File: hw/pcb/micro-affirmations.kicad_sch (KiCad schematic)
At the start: 18 parts, among them J1 USB-C_2171750001, J2 DEBUG, SW1 SW_Push, U1 STM32C031C6Tx

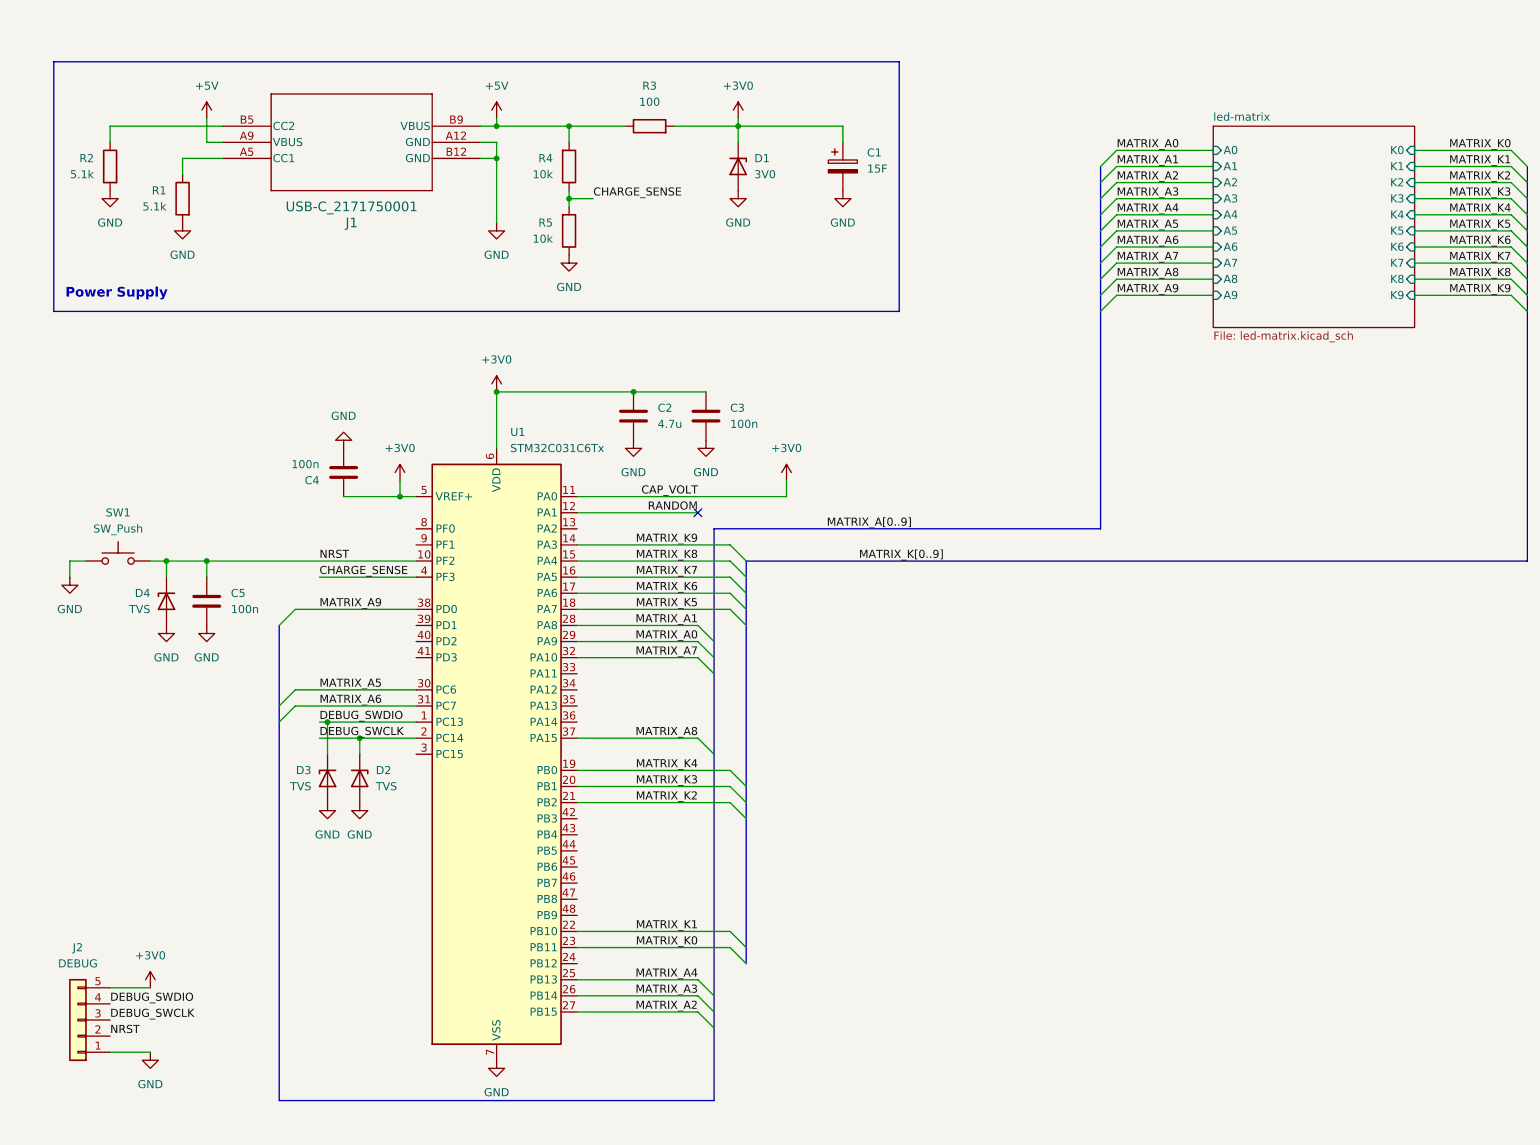
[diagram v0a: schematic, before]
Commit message: chore: redesigned pcb, new capacitor charger and smaller matrix
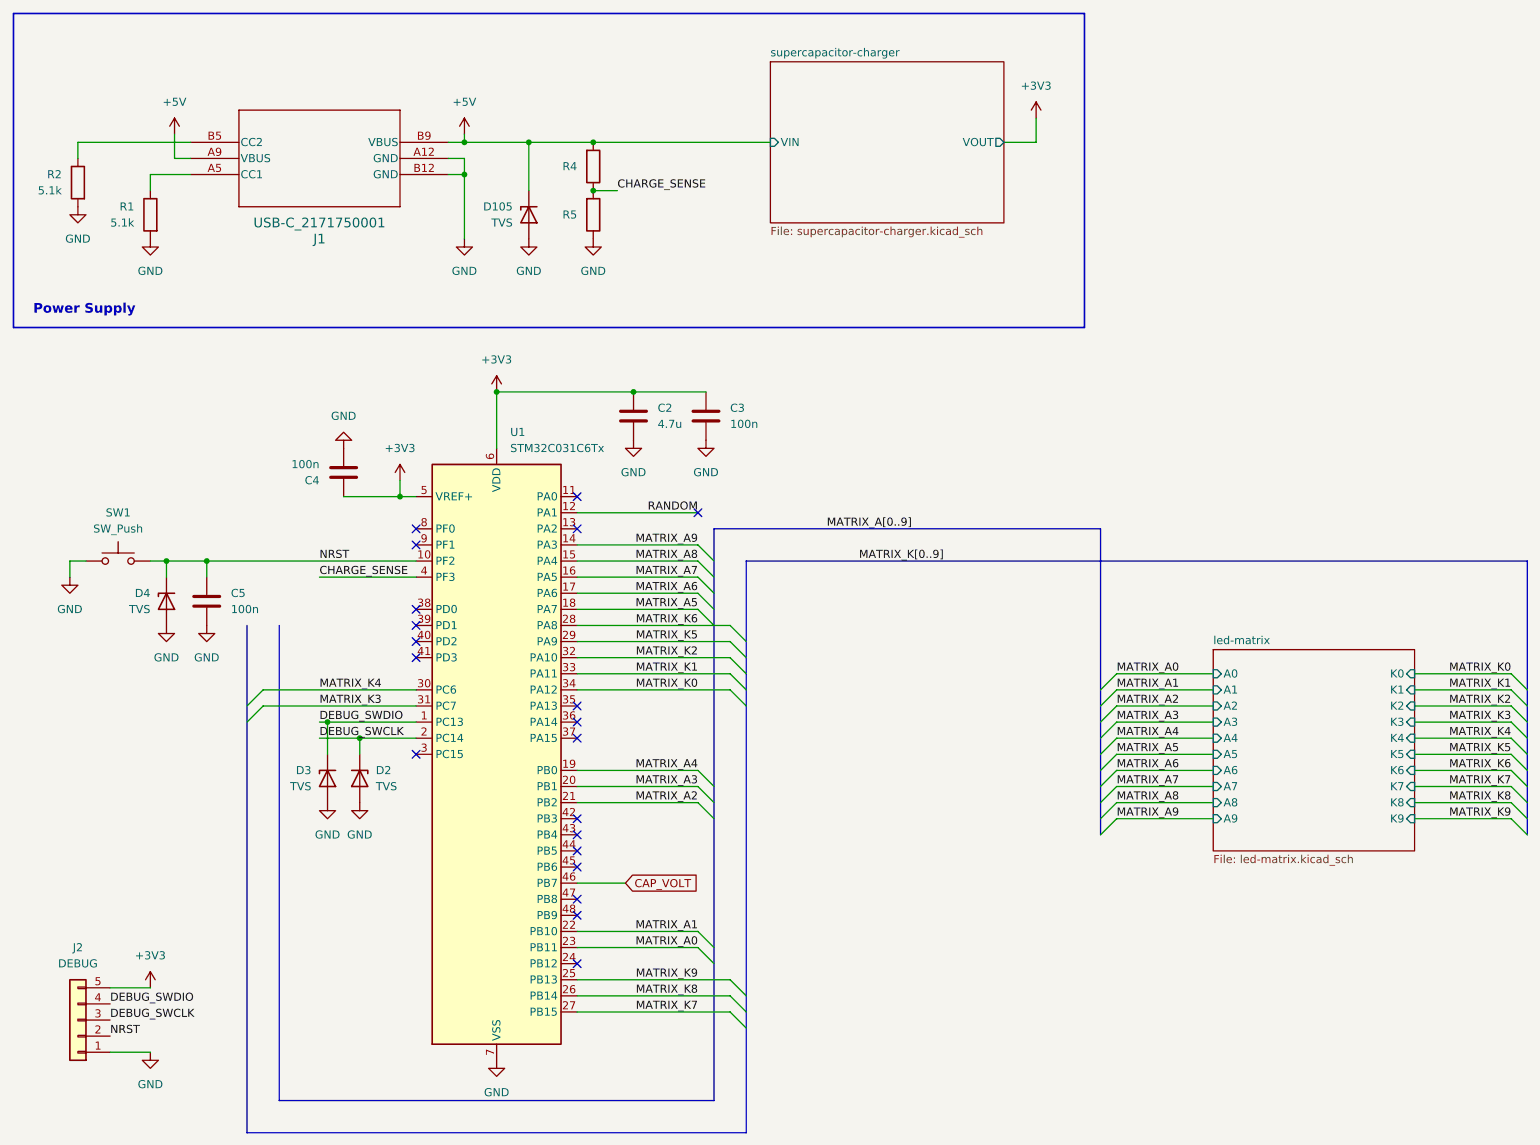
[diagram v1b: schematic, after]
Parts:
- removed C1: 15F, micro-affirmations_footprints:CP_Radial_L32.0mm_D12.5mm_P5.00mm_Horizontal, symbol Device:C_Polarized
- removed D1: 3V0, Diode_SMD:D_SOD-323, symbol Device:D_Zener
- removed R3: 100, Resistor_SMD:R_0603_1608Metric, symbol Device:R
- added D105: TVS, Diode_SMD:D_SOD-923, symbol Device:D_Zener
- D2, D3, D4: PN (none) -> ESD9L5.0ST5G
- R4, R5: value 10k -> (none)
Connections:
- net +5V: now also D105.1 (K)
- net GND: now also D105.2 (A)
- net MATRIX_A0: now also U1.23 (PB11); no longer U1.29 (PA9)
- net MATRIX_A1: now also U1.22 (PB10); no longer U1.28 (PA8)
- net MATRIX_A2: now also U1.21 (PB2); no longer U1.27 (PB15)
- net MATRIX_A3: now also U1.20 (PB1); no longer U1.26 (PB14)
- net MATRIX_A4: now also U1.19 (PB0); no longer U1.25 (PB13)
- net MATRIX_A5: now also U1.18 (PA7); no longer U1.30 (PC6)
- net MATRIX_A6: now also U1.17 (PA6); no longer U1.31 (PC7)
- net MATRIX_A7: now also U1.16 (PA5); no longer U1.32 (PA10)
- net MATRIX_A8: now also U1.15 (PA4); no longer U1.37 (PA15)
- net MATRIX_A9: now also U1.14 (PA3); no longer U1.38 (PD0)
- net MATRIX_K0: now also U1.34 (PA12); no longer U1.23 (PB11)
- net MATRIX_K1: now also U1.33 (PA11); no longer U1.22 (PB10)
- net MATRIX_K2: now also U1.32 (PA10); no longer U1.21 (PB2)
- net MATRIX_K3: now also U1.31 (PC7); no longer U1.20 (PB1)
- net MATRIX_K4: now also U1.30 (PC6); no longer U1.19 (PB0)
- net MATRIX_K5: now also U1.29 (PA9); no longer U1.18 (PA7)
- net MATRIX_K6: now also U1.28 (PA8); no longer U1.17 (PA6)
- net MATRIX_K7: now also U1.27 (PB15); no longer U1.16 (PA5)
- net MATRIX_K8: now also U1.26 (PB14); no longer U1.15 (PA4)
- net MATRIX_K9: now also U1.25 (PB13); no longer U1.14 (PA3)
- net CAP_VOLT: now reaches U1.46 (PB7)
- net +3V0 renamed +3V3
- net +3V3: no longer U1.11 (PA0)
- no-connect marks 1 -> 20
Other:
- added sheet supercapacitor-charger (supercapacitor-charger.kicad_sch)
- moved on the sheet: J1, R1, R2, R4, R5

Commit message: chore: updated schematics to show true part numbers
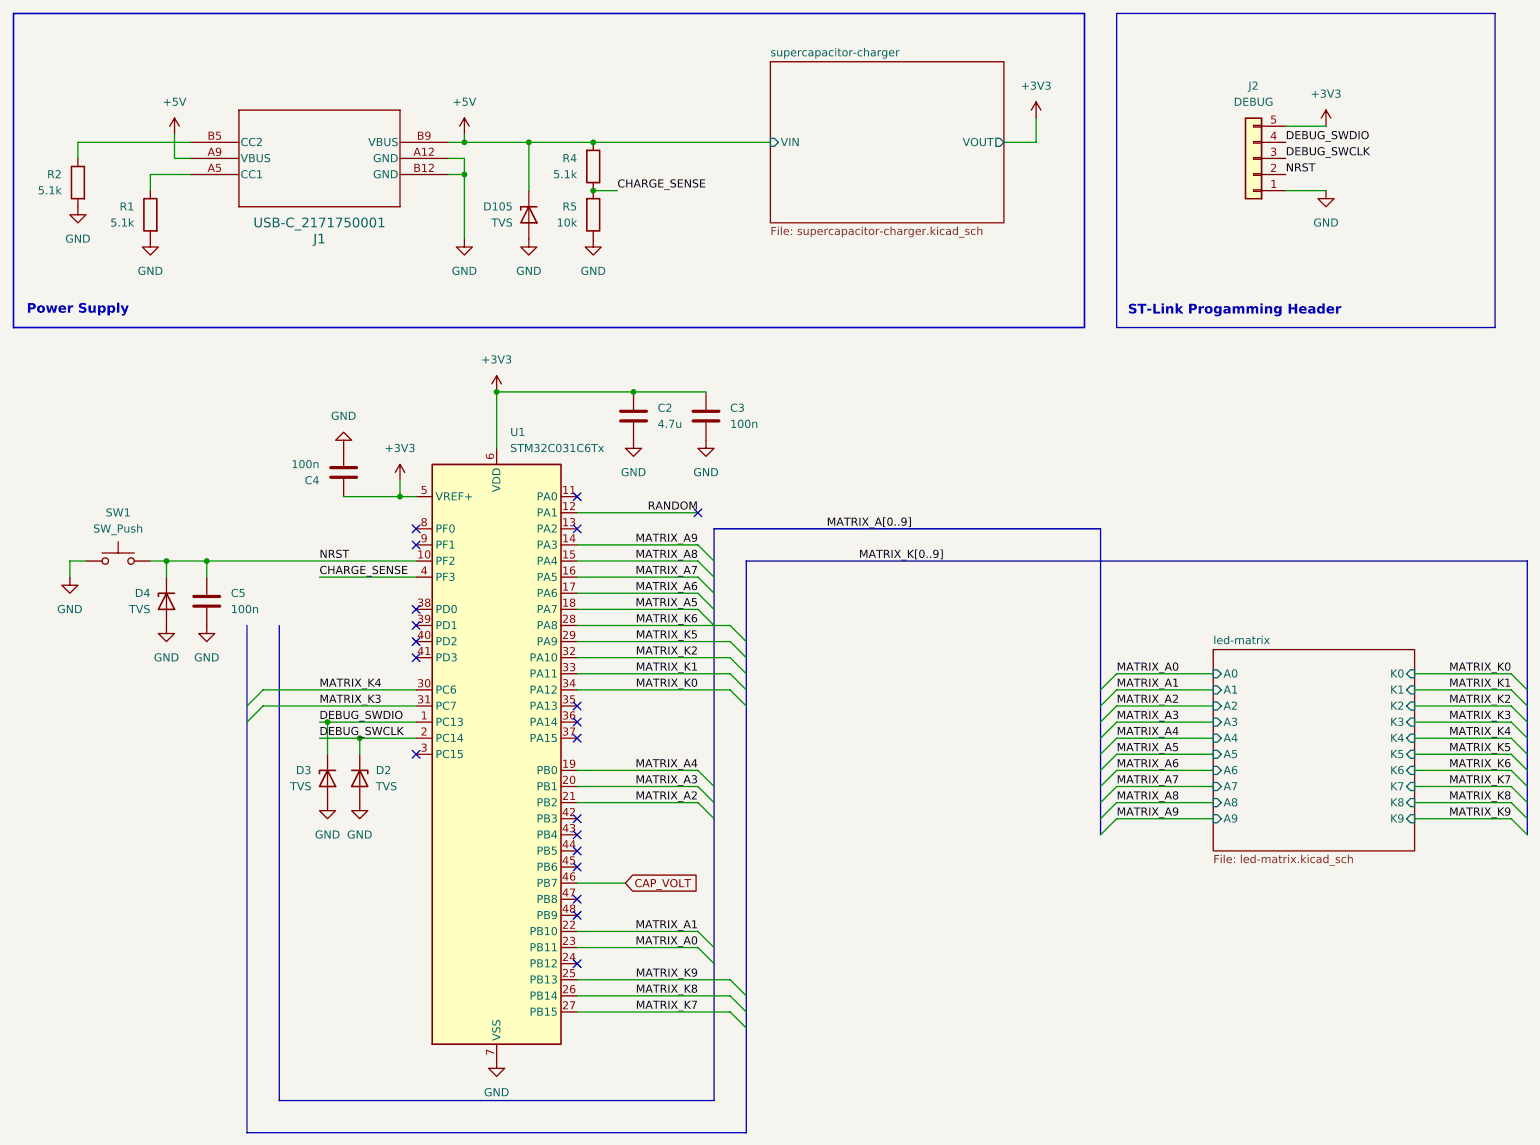
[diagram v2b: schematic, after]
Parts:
- C2: PN (none) -> C0805C475K4RACTU
- C3, C4, C5: PN (none) -> C0805F104K1RACAUTO
- J1: PN (none) -> 2171750001
- R1, R2: PN (none) -> CRG0603F5K1
- R4: value (none) -> 5.1k; PN (none) -> CRG0603F5K1
- R5: value (none) -> 10k; PN (none) -> CRGCQ0603F10K
- SW1: PN (none) -> TL1030AF350AQJ
- U1: PN (none) -> STM32C031C6T6TR
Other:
- note added: "ST-Link Progamming Header"
- moved on the sheet: J2
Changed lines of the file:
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@@
 		)
 	)
+	(rectangle
+		(start 190.5 16.51)
+		(end 250.19 66.04)
+		(stroke
+			(width 0)
+			(type default)
+		)
+		(fill
+			(type none)
+		)
+	)
+	(text "ST-Link Progamming Header"
+		(exclude_from_sim no)
+		(at 192.278 64.262 0)
+		(effects
+			(font
+				(size 1.524 1.524)
+				(thickness 0.254)
+				(bold yes)
+			)
+			(justify left bottom)
+		)
+	)
 	(text "Power Supply"
 		(exclude_from_sim no)
-		(at 27.686 63.246 0)
+		(at 26.67 63.246 0)
 		(effects
 			(font
@@
 	(wire
 		(pts
-			(xy 38.1 180.34) (xy 31.75 180.34)
+			(xy 223.52 44.45) (xy 217.17 44.45)
 		)
 		(stroke
@@
 	(wire
 		(pts
-			(xy 38.1 170.18) (xy 31.75 170.18)
+			(xy 223.52 34.29) (xy 217.17 34.29)
 		)
 		(stroke
@@
 	)
 	(label "DEBUG_SWDIO"
-		(at 31.75 172.72 0)
+		(at 217.17 36.83 0)
 		(effects
 			(font
@@
 	)
 	(label "DEBUG_SWCLK"
-		(at 31.75 175.26 0)
+		(at 217.17 39.37 0)
 		(effects
 			(font
@@
 	)
 	(label "NRST"
-		(at 31.75 177.8 0)
+		(at 217.17 41.91 0)
 		(effects
 			(font
@@
 			)
 		)
+		(property "PN" "CRG0603F5K1"
+			(at 26.67 43.18 0)
+			(hide yes)
+			(show_name no)
+			(do_not_autoplace no)
+			(effects
+				(font
+					(size 1.27 1.27)
+				)
+			)
+		)
 		(pin "1"
 		)
@@
 		(fields_autoplaced yes)
 		(property "Reference" "R4"
-			(at 105.41 40.6399 0)
+			(at 105.41 39.3699 0)
 			(show_name no)
 			(do_not_autoplace no)
@@
 			)
 		)
-		(property "Value" ""
+		(property "Value" "5.1k"
 			(at 105.41 41.9099 0)
 			(show_name no)
@@
 			)
 		)
+		(property "PN" "CRG0603F5K1"
+			(at 107.95 40.64 0)
+			(hide yes)
+			(show_name no)
+			(do_not_autoplace no)
+			(effects
+				(font
+					(size 1.27 1.27)
+				)
+			)
+		)
 		(pin "2"
 		)
@@
 			)
 		)
+		(property "PN" "STM32C031C6T6TR"
+			(at 92.71 133.35 0)
+			(hide yes)
+			(show_name no)
+			(do_not_autoplace no)
+			(effects
+				(font
+					(size 1.27 1.27)
+				)
+			)
+		)
 		(pin "36"
 		)
@@
 			)
 		)
+		(property "PN" "CRG0603F5K1"
+			(at 38.1 48.26 0)
+			(hide yes)
+			(show_name no)
+			(do_not_autoplace no)
+			(effects
+				(font
+					(size 1.27 1.27)
+				)
+			)
+		)
 		(pin "1"
 		)
@@
 			)
 		)
+		(property "PN" "TL1030AF350AQJ"
+			(at 33.02 102.87 0)
+			(hide yes)
+			(show_name no)
+			(do_not_autoplace no)
+			(effects
+				(font
+					(size 1.27 1.27)
+				)
+			)
+		)
 		(pin "2"
 		)
@@
 			)
 		)
+		(property "PN" "C0805F104K1RACAUTO"
+			(at 68.58 88.9 0)
+			(hide yes)
+			(show_name no)
+			(do_not_autoplace no)
+			(effects
+				(font
+					(size 1.27 1.27)
+				)
+			)
+		)
 		(pin "1"
 		)
@@
 			)
 		)
+		(property "PN" "C0805F104K1RACAUTO"
+			(at 125.73 80.01 0)
+			(hide yes)
+			(show_name no)
+			(do_not_autoplace no)
+			(effects
+				(font
+					(size 1.27 1.27)
+				)
+			)
+		)
 		(pin "1"
 		)
@@
 		(fields_autoplaced yes)
 		(property "Reference" "R5"
-			(at 105.41 48.2599 0)
+			(at 105.41 46.9899 0)
 			(show_name no)
 			(do_not_autoplace no)
@@
 			)
 		)
-		(property "Value" ""
+		(property "Value" "10k"
 			(at 105.41 49.5299 0)
 			(show_name no)
@@
 			)
 		)
+		(property "PN" "CRGCQ0603F10K"
+			(at 107.95 48.26 0)
+			(hide yes)
+			(show_name no)
+			(do_not_autoplace no)
+			(effects
+				(font
+					(size 1.27 1.27)
+				)
+			)
+		)
 		(pin "2"
 		)
@@
 			)
 		)
+		(property "PN" "C0805F104K1RACAUTO"
+			(at 46.99 109.22 0)
+			(hide yes)
+			(show_name no)
+			(do_not_autoplace no)
+			(effects
+				(font
+					(size 1.27 1.27)
+				)
+			)
+		)
 		(pin "1"
 		)
@@
 			)
 		)
+		(property "PN" "2171750001"
+			(at 44.45 41.91 0)
+			(hide yes)
+			(show_name no)
+			(do_not_autoplace no)
+			(effects
+				(font
+					(size 1.27 1.27)
+				)
+			)
+		)
 		(pin "A5"
 		)
@@
 			)
 		)
+		(property "PN" "C0805C475K4RACTU"
+			(at 114.3 80.01 0)
+			(hide yes)
+			(show_name no)
+			(do_not_autoplace no)
+			(effects
+				(font
+					(size 1.27 1.27)
+				)
+			)
+		)
 		(pin "1"
 		)
@@
 	(symbol
 		(lib_id "Connector_Generic:Conn_01x05")
-		(at 26.67 175.26 180)
+		(at 212.09 39.37 180)
 		(unit 1)
 		(body_style 1)
@@
 		(fields_autoplaced yes)
 		(property "Reference" "J2"
-			(at 26.67 163.83 0)
+			(at 212.09 27.94 0)
 			(show_name no)
 			(do_not_autoplace no)
@@
 		)
 		(property "Value" "DEBUG"
-			(at 26.67 166.37 0)
+			(at 212.09 30.48 0)
 			(show_name no)
 			(do_not_autoplace no)
@@
 		)
 		(property "Footprint" "Connector_PinHeader_2.54mm:PinHeader_1x05_P2.54mm_Vertical"
-			(at 26.67 175.26 0)
+			(at 212.09 39.37 0)
 			(hide yes)
 			(show_name no)
@@
 		)
 		(property "Datasheet" ""
-			(at 26.67 175.26 0)
+			(at 212.09 39.37 0)
 			(hide yes)
 			(show_name no)
@@
 		)
 		(property "Description" "Generic connector, single row, 01x05, script generated (kicad-library-utils/schlib/autogen/connector/)"
-			(at 26.67 175.26 0)
+			(at 212.09 39.37 0)
 			(hide yes)
 			(show_name no)
@@
 	(symbol
 		(lib_id "power:GND")
-		(at 38.1 180.34 0)
+		(at 223.52 44.45 0)
 		(unit 1)
 		(body_style 1)
@@
 		(fields_autoplaced yes)
 		(property "Reference" "#PWR032"
-			(at 38.1 186.69 0)
+			(at 223.52 50.8 0)
 			(hide yes)
 			(show_name no)
@@
 		)
 		(property "Value" "GND"
-			(at 38.1 185.42 0)
+			(at 223.52 49.53 0)
 			(show_name no)
 			(do_not_autoplace no)
@@
 		)
 		(property "Footprint" ""
-			(at 38.1 180.34 0)
+			(at 223.52 44.45 0)
 			(hide yes)
 			(show_name no)
@@
 		)
 		(property "Datasheet" ""
-			(at 38.1 180.34 0)
+			(at 223.52 44.45 0)
 			(hide yes)
 			(show_name no)
@@
 		)
 		(property "Description" "Power symbol creates a global label with name \"GND\" , ground"
-			(at 38.1 180.34 0)
+			(at 223.52 44.45 0)
 			(hide yes)
 			(show_name no)
@@
 	(symbol
 		(lib_id "power:+3V3")
-		(at 38.1 170.18 0)
+		(at 223.52 34.29 0)
 		(unit 1)
 		(body_style 1)
@@
 		(fields_autoplaced yes)
 		(property "Reference" "#PWR033"
-			(at 38.1 173.99 0)
+			(at 223.52 38.1 0)
 			(hide yes)
 			(show_name no)
@@
 		)
 		(property "Value" "+3V3"
-			(at 38.1 165.1 0)
+			(at 223.52 29.21 0)
 			(show_name no)
 			(do_not_autoplace no)
@@
 		)
 		(property "Footprint" ""
-			(at 38.1 170.18 0)
+			(at 223.52 34.29 0)
 			(hide yes)
 			(show_name no)
@@
 		)
 		(property "Datasheet" ""
-			(at 38.1 170.18 0)
+			(at 223.52 34.29 0)
 			(hide yes)
 			(show_name no)
@@
 		)
 		(property "Description" "Power symbol creates a global label with name \"+3V3\""
-			(at 38.1 170.18 0)
+			(at 223.52 34.29 0)
 			(hide yes)
 			(show_name no)
